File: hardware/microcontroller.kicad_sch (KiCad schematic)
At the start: 18 parts, among them J5 1x2 jumper right-angle, J7 1x2 jumper right-angle, U15 decoder, U16 3.3V <=> 5V, U17 decoder

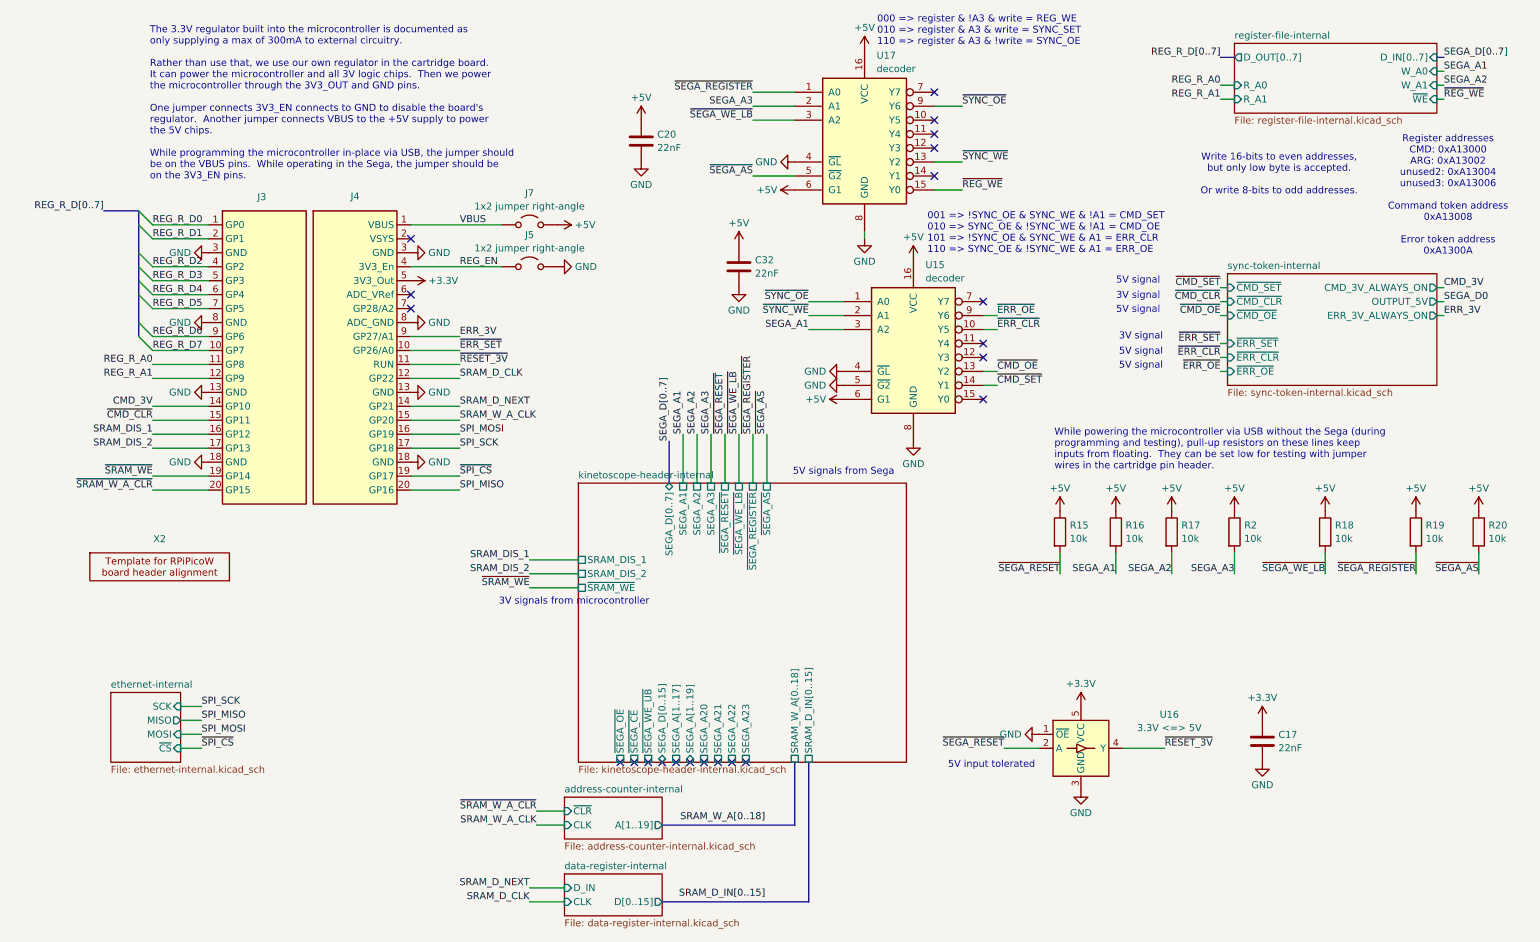
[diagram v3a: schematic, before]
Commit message: Revise microcontroller board based on latest cart board improvements
 - Update comments
 - Segregate the Ethernet module's power supply so it can be
   disconnected if something goes wrong in a prototype
 - Update board setup to match latest cart board
 - Remove unnecessary level-shifter
 - Fix address decoder to non-latching version
 - Fix address decoder output assignment
 - Consolidate buffer ICs in register file
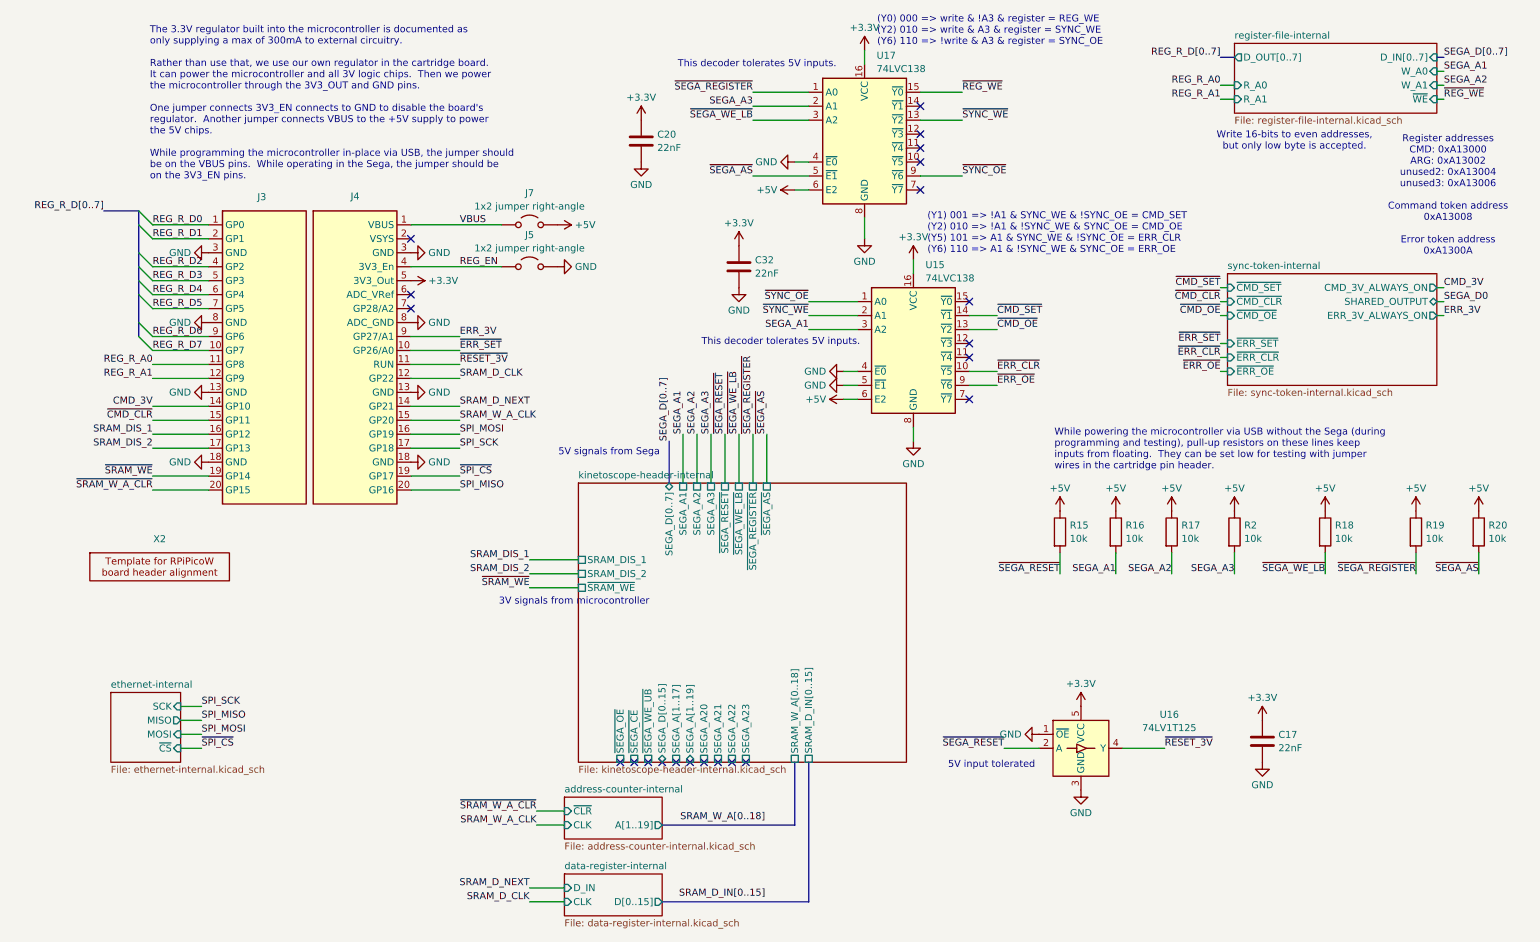
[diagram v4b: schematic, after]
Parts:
- U15, U17: value decoder -> 74LVC138; footprint Package_SO:SO-16_3.9x9.9mm_P1.27mm -> Package_SO:TSSOP-16_4.4x5mm_P0.65mm; symbol 74xx:74LS137 -> 74xx:74HC138; JLCPCB Part Number C17116 -> C6062; Mouser Part Number 771-74HC137D-T -> 771-74LVC138APW-T; Part Number 74HC137D,653 -> 74LVC138APW,118
- U16: value 3.3V <=> 5V -> 74LV1T125
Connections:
- net +3.3V: now also C20.1, C32.1, U15.16 (VCC), U17.16 (VCC)
- net +5V: no longer C20.1, C32.1, U15.16 (VCC), U17.16 (VCC)
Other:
- sheet sync-token-internal ports: added SHARED_OUTPUT; removed OUTPUT_5V
- note added: "(Y0) 000 => write & !A3 & register = REG_WE (Y2) 010 => write & A3 & register = SYNC_WE (Y6) 110 => !write & A3 & register = SYNC_OE"
- note added: "(Y1) 001 => !A1 & SYNC_WE & !SYNC_OE = CMD_SET (Y2) 010 => !A1 & !SYNC_WE & SYNC_OE = CMD_OE (Y5) 101 => A1 & SYNC_WE & !SYNC_OE = ERR_CLR (Y6) 110 => A1 & !SYNC_WE & SYNC_OE = ERR_OE"
- note added: "This decoder tolerates 5V inputs."
- note added: "Write 16-bits to even addresses, but only low byte is accepted."
- note removed: "000 => register & !A3 & write = REG_WE 010 => register & A3 & write = SYNC_SET 110 => register & A3 & !write = SYNC_OE"
- note removed: "001 => !SYNC_OE & SYNC_WE & !A1 = CMD_SET 010 => SYNC_OE & !SYNC_WE & !A1 = CMD_OE 101 => !SYNC_OE & SYNC_WE & A1 = ERR_CLR 110 => SYNC_OE & !SYNC_WE & A1 = ERR_OE"
- note removed: "3V signal"
- note removed: "5V signal"
- note removed: "Write 16-bits to even addresses, but only low byte is accepted. Or write 8-bits to odd addresses."

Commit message: Remove ethernet module, add pin header for Adafruit Ethernet featherwing instead
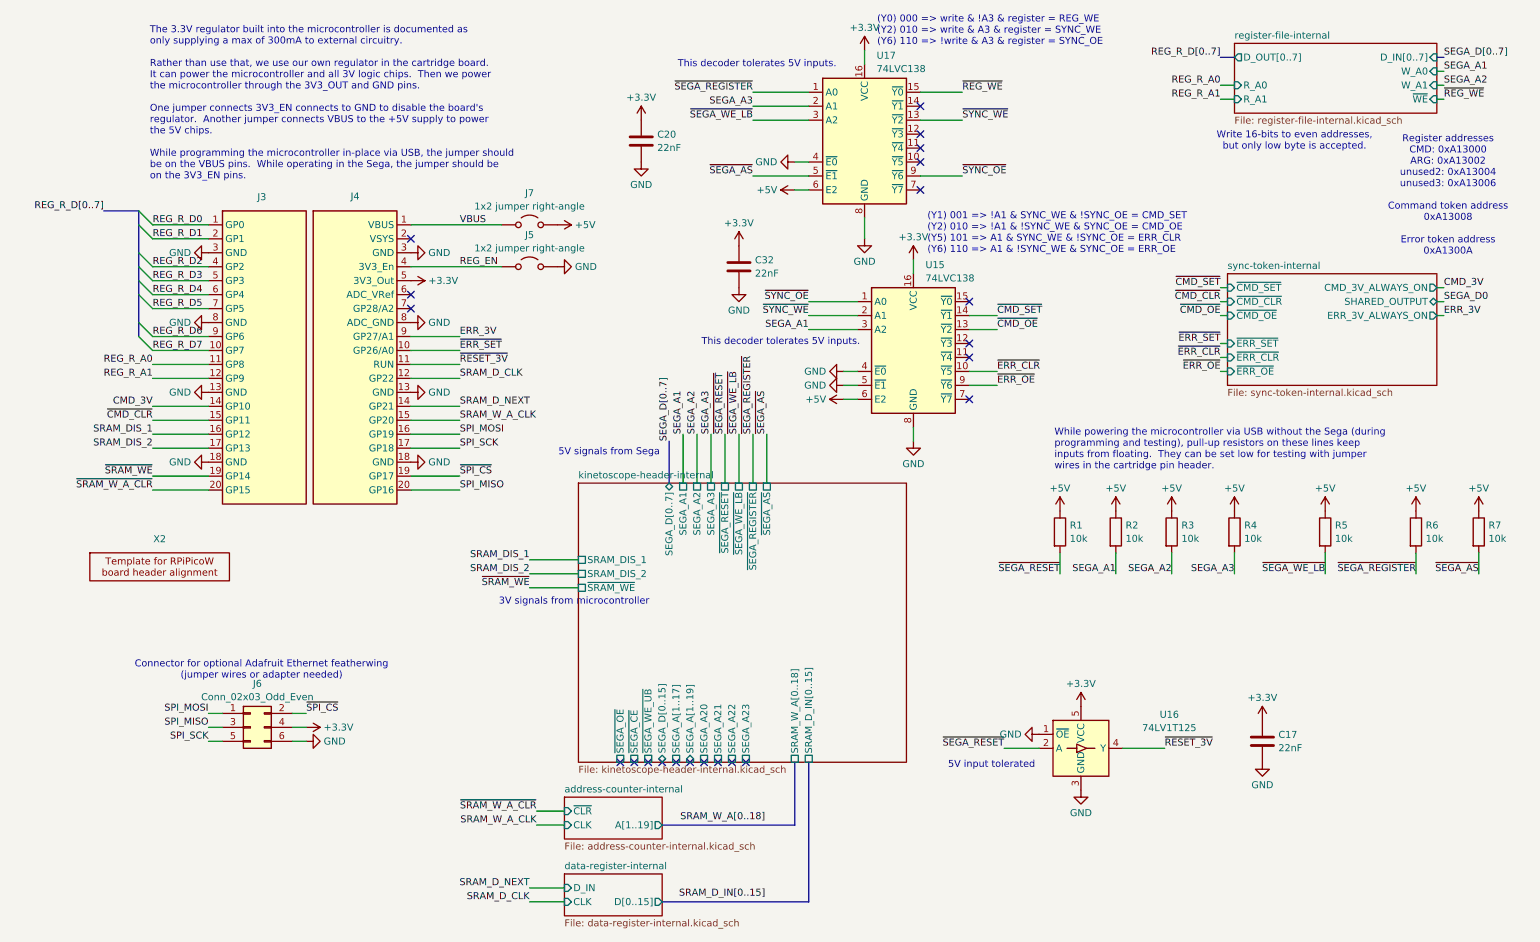
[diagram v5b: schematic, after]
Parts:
- added J6: Conn_02x03_Odd_Even, Connector_PinHeader_2.54mm:PinHeader_2x03_P2.54mm_Vertical, symbol Connector_Generic:Conn_02x03_Odd_Even
- renumbered R15 to R1, R16 to R2, R17 to R3, R2 to R4, R18 to R5, R19 to R6, R20 to R7
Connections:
- net +3.3V: now also J6.4 (Pin_4)
- net GND: now also J6.6 (Pin_6)
- net SPI_MISO: now also J6.3 (Pin_3)
- net SPI_MOSI: now also J6.1 (Pin_1)
- net SPI_SCK: now also J6.5 (Pin_5)
- net ~{SPI_CS}: now also J6.2 (Pin_2)
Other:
- removed sheet ethernet-internal
- note added: "Connector for optional Adafruit Ethernet featherwing (jumper wires or adapter needed)"

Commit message: Revise microcontroller board based on latest cart board improvements
 - Update comments
 - Segregate the Ethernet module's power supply so it can be
   disconnected if something goes wrong in a prototype
 - Update board setup to match latest cart board
 - Remove unnecessary level-shifter
 - Fix address decoder to non-latching version
 - Fix address decoder output assignment
 - Consolidate buffer ICs in register file
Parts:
- J3, J4: Part Number (none) -> 61302011821
- J5, J7: Part Number (none) -> PH1RB-02-UA
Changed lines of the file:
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@@
+			)
+		)
+		(property "Part Number" "PH1RB-02-UA"
+			(at 104.14 58.42 0)
+			(effects
+				(font
+					(size 1.27 1.27)
+				)
+				(hide yes)
 			)
 		)
@@
 			)
 		)
+		(property "Part Number" "61302011821"
+			(at 55.88 48.26 0)
+			(effects
+				(font
+					(size 1.27 1.27)
+				)
+				(hide yes)
+			)
+		)
 		(pin "17"
 		)
@@
 			)
 		)
+		(property "Part Number" "61302011821"
+			(at 72.39 48.26 0)
+			(effects
+				(font
+					(size 1.27 1.27)
+				)
+				(hide yes)
+			)
+		)
 		(pin "18"
 		)
@@
 			(at 104.14 50.8 0)
 			(effects
+				(font
+					(size 1.27 1.27)
+				)
+				(hide yes)
+			)
+		)
+		(property "Part Number" "PH1RB-02-UA"
+			(at 104.14 50.8 0)
+			(effects

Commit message: Replace address counters with slightly larger versions that can be assembled more easily
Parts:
- J5, J7: JLCPCB Part Number C5540789 -> (none)
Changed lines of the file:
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@@
 			)
 		)
-		(property "JLCPCB Part Number" "C5540789"
+		(property "JLCPCB Part Number" ""
 			(at 104.14 58.42 0)
 			(effects
@@
 			)
 		)
-		(property "JLCPCB Part Number" "C5540789"
+		(property "JLCPCB Part Number" ""
 			(at 104.14 50.8 0)
 			(effects

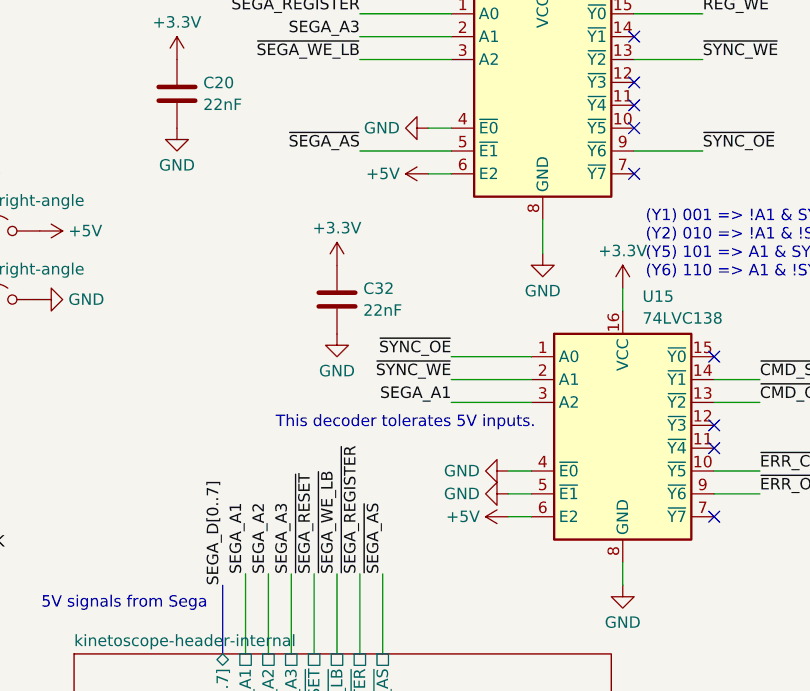
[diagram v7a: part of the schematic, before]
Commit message: Fix voltage for hard-coded values in microcontroller address decoder
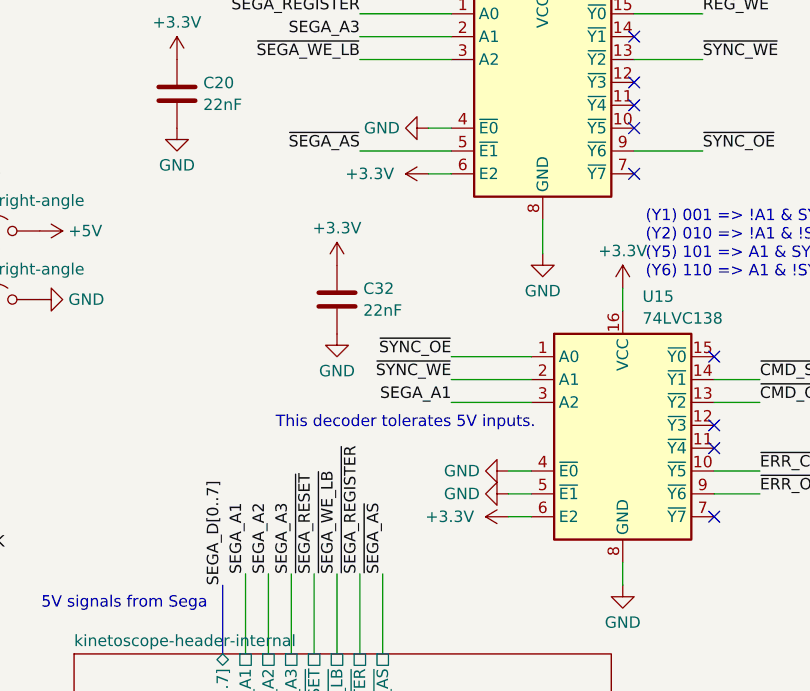
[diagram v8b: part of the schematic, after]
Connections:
- net +3.3V: now also U15.6 (E2), U17.6 (E2)
- net +5V: no longer U15.6 (E2), U17.6 (E2)
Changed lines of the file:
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@@
+	(symbol
+		(lib_id "power:+3.3V")
+		(at 161.29 82.55 90)
+		(unit 1)
+		(exclude_from_sim no)
+		(in_bom yes)
+		(on_board yes)
+		(dnp no)
+		(fields_autoplaced yes)
+		(property "Reference" "#PWR065"
+			(at 165.1 82.55 0)
+			(effects
+				(font
+					(size 1.27 1.27)
+				)
+				(hide yes)
+			)
+		)
+		(property "Value" "+3.3V"
+			(at 157.48 82.5499 90)
+			(effects
+				(font
+					(size 1.27 1.27)
+				)
+				(justify left)
+			)
+		)
+		(property "Footprint" ""
+			(at 161.29 82.55 0)
+			(effects
+				(font
+					(size 1.27 1.27)
+				)
+				(hide yes)
+			)
+		)
+		(property "Datasheet" ""
+			(at 161.29 82.55 0)
+			(effects
+				(font
+					(size 1.27 1.27)
+				)
+				(hide yes)
+			)
+		)
+		(property "Description" "Power symbol creates a global label with name \"+3.3V\""
+			(at 161.29 82.55 0)
+			(effects
+				(font
+					(size 1.27 1.27)
+				)
+				(hide yes)
+			)
+		)
+		(pin "1"
+		)
+		(instances
+			(project "microcontroller"
+				(path "/eb0e957f-b2ea-4261-97c1-e28148a3f6e1"
+					(reference "#PWR065")
+					(unit 1)
+				)
+			)
+		)
+	)
 	(symbol
 		(lib_id "power:+3.3V")
@@
 	)
 	(symbol
-		(lib_id "power:+5V")
-		(at 161.29 82.55 90)
-		(unit 1)
-		(exclude_from_sim no)
-		(in_bom yes)
-		(on_board yes)
-		(dnp no)
-		(fields_autoplaced yes)
-		(property "Reference" "#PWR0131"
-			(at 165.1 82.55 0)
-			(effects
-				(font
-					(size 1.27 1.27)
-				)
-				(hide yes)
-			)
-		)
-		(property "Value" "+5V"
-			(at 158.1151 82.55 90)
-			(effects
-				(font
-					(size 1.27 1.27)
-				)
-				(justify left)
-			)
-		)
-		(property "Footprint" ""
-			(at 161.29 82.55 0)
-			(effects
-				(font
-					(size 1.27 1.27)
-				)
-				(hide yes)
-			)
-		)
-		(property "Datasheet" ""
-			(at 161.29 82.55 0)
-			(effects
-				(font
-					(size 1.27 1.27)
-				)
-				(hide yes)
-			)
-		)
-		(property "Description" "Power symbol creates a global label with name \"+5V\""
-			(at 161.29 82.55 0)
-			(effects
-				(font
-					(size 1.27 1.27)
-				)
-				(hide yes)
-			)
-		)
-		(pin "1"
-		)
-		(instances
-			(project "microcontroller"
-				(path "/eb0e957f-b2ea-4261-97c1-e28148a3f6e1"
-					(reference "#PWR0131")
-					(unit 1)
-				)
-			)
-		)
-	)
-	(symbol
 		(lib_id "power:GND")
 		(at 82.55 68.58 90)
@@
 	)
 	(symbol
+		(lib_id "power:+3.3V")
+		(at 152.4 44.45 90)
+		(unit 1)
+		(exclude_from_sim no)
+		(in_bom yes)
+		(on_board yes)
+		(dnp no)
+		(fields_autoplaced yes)
+		(property "Reference" "#PWR064"
+			(at 156.21 44.45 0)
+			(effects
+				(font
+					(size 1.27 1.27)
+				)
+				(hide yes)
+			)
+		)
+		(property "Value" "+3.3V"
+			(at 148.59 44.4499 90)
+			(effects
+				(font
+					(size 1.27 1.27)
+				)
+				(justify left)
+			)
+		)
+		(property "Footprint" ""
+			(at 152.4 44.45 0)
+			(effects
+				(font
+					(size 1.27 1.27)
+				)
+				(hide yes)
+			)
+		)
+		(property "Datasheet" ""
+			(at 152.4 44.45 0)
+			(effects
+				(font
+					(size 1.27 1.27)
+				)
+				(hide yes)
+			)
+		)
+		(property "Description" "Power symbol creates a global label with name \"+3.3V\""
+			(at 152.4 44.45 0)
+			(effects
+				(font
+					(size 1.27 1.27)
+				)
+				(hide yes)
+			)
+		)
+		(pin "1"
+		)
+		(instances
+			(project "microcontroller"
+				(path "/eb0e957f-b2ea-4261-97c1-e28148a3f6e1"
+					(reference "#PWR064")
+					(unit 1)
+				)
+			)
+		)
+	)
+	(symbol
 		(lib_id "power:GND")
 		(at 152.4 39.37 270)
@@
 					(unit 1)
 				)
-			)
-		)
-	)
-	(symbol
-		(lib_id "power:+5V")
-		(at 152.4 44.45 90)
-		(unit 1)
-		(exclude_from_sim no)
-		(in_bom yes)
-		(on_board yes)
-		(dnp no)
-		(fields_autoplaced yes)
-		(property "Reference" "#PWR082"
-			(at 156.21 44.45 0)
-			(effects
-				(font
-					(size 1.27 1.27)
-				)
-				(hide yes)
-			)
-		)
-		(property "Value" "+5V"
-			(at 149.2251 44.45 90)
-			(effects
-				(font
-					(size 1.27 1.27)
-				)
-				(justify left)
-			)
-		)
-		(property "Footprint" ""
-			(at 152.4 44.45 0)
-			(effects
-				(font
-					(size 1.27 1.27)
-				)
-				(hide yes)
-			)
-		)
-		(property "Datasheet" ""
-			(at 152.4 44.45 0)
-			(effects
-				(font
-					(size 1.27 1.27)
-				)
-				(hide yes)
-			)
-		)
-		(property "Description" "Power symbol creates a global label with name \"+5V\""
-			(at 152.4 44.45 0)
-			(effects
-				(font
-					(size 1.27 1.27)
-				)
-				(hide yes)
-			)
-		)
-		(pin "1"
-		)
-		(instances
-			(project "microcontroller"
-				(path "/eb0e957f-b2ea-4261-97c1-e28148a3f6e1"
-					(reference "#PWR082")
-					(unit 1)
-				)
